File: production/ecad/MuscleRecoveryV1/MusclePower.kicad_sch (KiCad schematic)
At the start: 23 parts, among them IC1 LC709203FQH-01TWG, Q1 FDN340P, U1 AP1117-33, U2 MCP73831-2-OT

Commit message: rev1 first draft ready for review
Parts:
- removed R34, R35: 10K, symbol Device:R
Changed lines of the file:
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@@
   (junction (at 144.145 44.45) (diameter 0) (color 0 0 0 0)
   )
-  (junction (at 66.04 113.03) (diameter 0) (color 0 0 0 0)
-  )
   (junction (at 165.735 49.53) (diameter 0) (color 0 0 0 0)
   )
@@
   )
   (junction (at 95.25 51.7144) (diameter 0) (color 0 0 0 0)
-  )
-  (junction (at 69.85 115.57) (diameter 0) (color 0 0 0 0)
-  )
-  (junction (at 69.85 96.52) (diameter 0) (color 0 0 0 0)
   )
   (junction (at 50.8 54.0004) (diameter 0) (color 0 0 0 0)
@@
     (stroke (width 0) (type default))
   )
-  (wire (pts (xy 59.69 113.03) (xy 66.04 113.03))
+  (wire (pts (xy 59.69 113.03) (xy 71.12 113.03))
     (stroke (width 0) (type default))
   )
@@
     (stroke (width 0) (type default))
   )
-  (wire (pts (xy 66.04 113.03) (xy 71.12 113.03))
-    (stroke (width 0) (type default))
-  )
   (wire (pts (xy 36.83 114.3) (xy 36.83 116.84))
     (stroke (width 0) (type default))
@@
     (stroke (width 0) (type default))
   )
-  (wire (pts (xy 69.85 96.52) (xy 69.85 102.87))
-    (stroke (width 0) (type default))
-  )
   (wire (pts (xy 50.8 53.848) (xy 50.8 54.0004))
     (stroke (width 0) (type default))
@@
     (stroke (width 0) (type default))
   )
-  (wire (pts (xy 66.04 100.33) (xy 66.04 96.52))
-    (stroke (width 0) (type default))
-  )
   (wire (pts (xy 97.79 96.52) (xy 97.79 102.87))
     (stroke (width 0) (type default))
@@
     (stroke (width 0) (type default))
   )
-  (wire (pts (xy 66.04 107.95) (xy 66.04 113.03))
-    (stroke (width 0) (type default))
-  )
   (wire (pts (xy 27.94 65.6844) (xy 27.94 62.23))
     (stroke (width 0) (type default))
   )
-  (wire (pts (xy 69.85 115.57) (xy 71.12 115.57))
-    (stroke (width 0) (type default))
-  )
   (wire (pts (xy 71.12 120.65) (xy 67.31 120.65))
     (stroke (width 0) (type default))
@@
     (stroke (width 0) (type default))
   )
-  (wire (pts (xy 69.85 96.52) (xy 81.28 96.52))
-    (stroke (width 0) (type default))
-  )
-  (wire (pts (xy 66.04 96.52) (xy 69.85 96.52))
-    (stroke (width 0) (type default))
-  )
   (wire (pts (xy 46.99 116.84) (xy 46.99 121.92))
     (stroke (width 0) (type default))
@@
     (stroke (width 0) (type default))
   )
-  (wire (pts (xy 69.85 110.49) (xy 69.85 115.57))
-    (stroke (width 0) (type default))
-  )
   (wire (pts (xy 27.9908 48.26) (xy 43.18 48.26))
     (stroke (width 0) (type default))
@@
     (stroke (width 0) (type default))
   )
-  (wire (pts (xy 59.69 115.57) (xy 69.85 115.57))
+  (wire (pts (xy 59.69 115.57) (xy 71.12 115.57))
     (stroke (width 0) (type default))
   )
@@
         (path "/ec7ffed6-1d2d-48f7-b073-d0a7d4b8c858"
           (reference "#PWR04") (unit 1)
-        )
-      )
-    )
-  )
-  (symbol (lib_id "Device:R") (at 66.04 104.14 0) (unit 1)
-    (in_bom yes) (on_board yes) (dnp no)
-    (property "Reference" "R34" (at 62.23 102.87 0)
-      (effects (font (size 1.27 1.27)) (justify left))
-    )
-    (property "Value" "10K" (at 60.96 105.41 0)
-      (effects (font (size 1.27 1.27)) (justify left))
-    )
-    (property "Footprint" "" (at 64.262 104.14 90)
-      (effects (font (size 1.27 1.27)) hide)
-    )
-    (property "Datasheet" "~" (at 66.04 104.14 0)
-      (effects (font (size 1.27 1.27)) hide)
-    )
-    (pin "1")
-    (pin "2")
-    (instances
-      (project "MuscleRecoveryV1"
-        (path "/4e550305-79d2-4e4a-a502-817ebcc79f9a/648f095b-a230-48ff-8dbf-d0fbef398770"
-          (reference "R34") (unit 1)
         )
       )
@@
         )
       )
-    )
-  )
-  (symbol (lib_id "Device:R") (at 69.85 106.68 0) (unit 1)
-    (in_bom yes) (on_board yes) (dnp no)
-    (property "Reference" "R35" (at 71.12 105.41 0)
-      (effects (font (size 1.27 1.27)) (justify left))
-    )
-    (property "Value" "10K" (at 71.12 107.95 0)
-      (effects (font (size 1.27 1.27)) (justify left))
-    )
-    (property "Footprint" "" (at 68.072 106.68 90)
-      (effects (font (size 1.27 1.27)) hide)
-    )
-    (property "Datasheet" "~" (at 69.85 106.68 0)
-      (effects (font (size 1.27 1.27)) hide)
-    )
-    (pin "1")
-    (pin "2")
-    (instances
-      (project "MuscleRecoveryV1"
-        (path "/4e550305-79d2-4e4a-a502-817ebcc79f9a/648f095b-a230-48ff-8dbf-d0fbef398770"
-          (reference "R35") (unit 1)
-        )
-      )

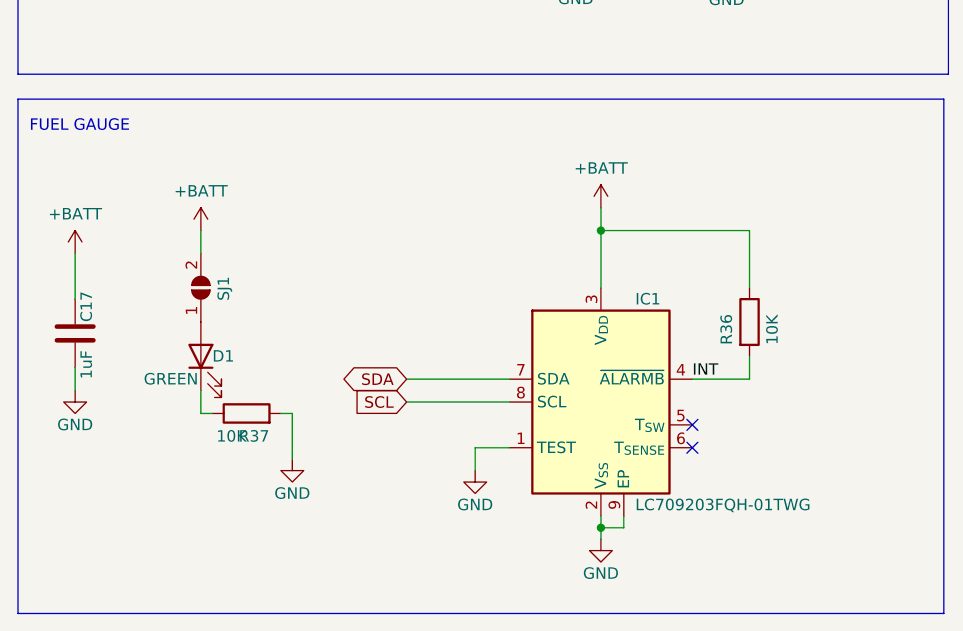
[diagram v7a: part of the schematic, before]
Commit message: updates from Sean's comments, some not all
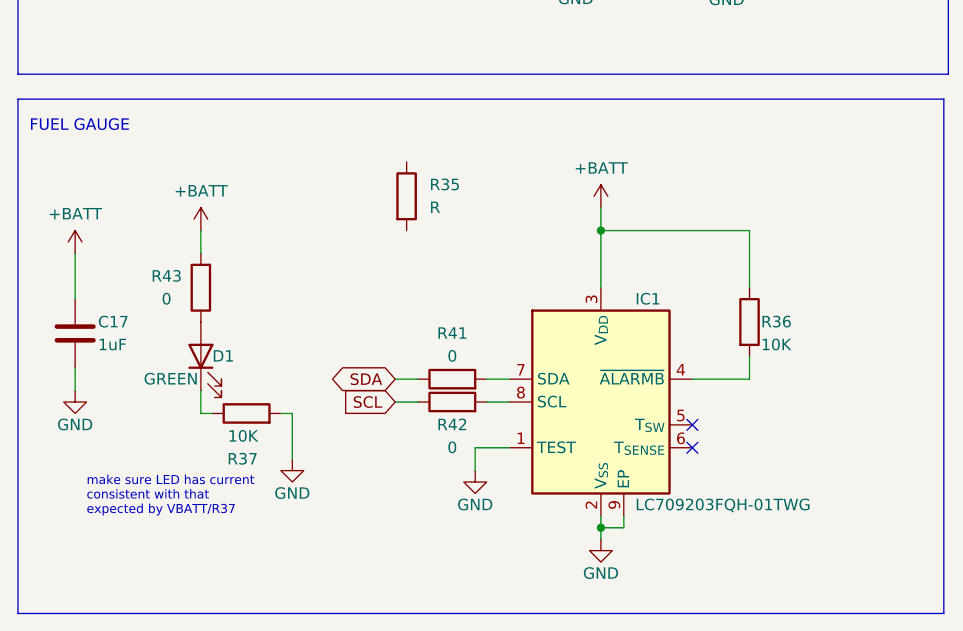
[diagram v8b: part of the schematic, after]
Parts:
- removed SJ1: SolderJumper_2_Open, symbol Jumper:SolderJumper_2_Open
- added R35: R, symbol Device:R
- added R41, R42, R43: 0, symbol Device:R
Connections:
- net +BATT: now also R43.2
- net SCL: now also R42.1; no longer IC1.8 (SCL)
- net SDA: now also R41.1; no longer IC1.7 (SDA)
- net at D1.2 (A): now also R43.1
- net INT: no longer names the net of IC1.4 (~{ALARMB}), R36.2
- new net: IC1.7 (SDA), R41.2
- new net: IC1.8 (SCL), R42.2
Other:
- note added: "make sure LED has current consistent with that expected by VBATT/R37"
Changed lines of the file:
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@@
-    (stroke (width 0) (type default))
-  )
-  (wire (pts (xy 59.69 113.03) (xy 71.12 113.03))
     (stroke (width 0) (type default))
   )
@@
     (stroke (width 0) (type default))
   )
+  (wire (pts (xy 68.58 113.03) (xy 71.12 113.03))
+    (stroke (width 0) (type default))
+  )
   (wire (pts (xy 95.25 60.96) (xy 95.25 66.04))
     (stroke (width 0) (type default))
@@
     (stroke (width 0) (type default))
   )
+  (wire (pts (xy 58.42 113.03) (xy 60.96 113.03))
+    (stroke (width 0) (type default))
+  )
   (wire (pts (xy 50.8 54.0004) (xy 69.342 54.0004))
     (stroke (width 0) (type default))
@@
     (stroke (width 0) (type default))
   )
+  (wire (pts (xy 68.58 115.57) (xy 71.12 115.57))
+    (stroke (width 0) (type default))
+  )
   (wire (pts (xy 27.94 65.6844) (xy 27.94 62.23))
     (stroke (width 0) (type default))
@@
     (stroke (width 0) (type default))
   )
+  (wire (pts (xy 58.42 115.57) (xy 60.96 115.57))
+    (stroke (width 0) (type default))
+  )
   (wire (pts (xy 46.99 116.84) (xy 46.99 121.92))
     (stroke (width 0) (type default))
@@
   )
   (wire (pts (xy 95.25 51.7144) (xy 95.25 55.88))
-    (stroke (width 0) (type default))
-  )
-  (wire (pts (xy 59.69 115.57) (xy 71.12 115.57))
     (stroke (width 0) (type default))
   )
@@
     (effects (font (size 1.27 1.27)) (justify left bottom))
   )
+  (text "make sure LED has current \nconsistent with that \nexpected by VBATT/R37"
+    (at 24.13 128.27 0)
+    (effects (font (size 1 1)) (justify left bottom))
+  )
   (text "Charging Circuitry\n" (at 126.365 20.701 0)
     (effects (font (size 1.27 1.27)) (justify left bottom))
   )
   (text "Power Selection Circuitry\n" (at 18.796 21.2344 0)
-    (effects (font (size 1.27 1.27)) (justify left bottom))
-  )
-  (label "INT" (at 91.44 113.03 0) (fields_autoplaced)
     (effects (font (size 1.27 1.27)) (justify left bottom))
   )
@@
     )
   )
-  (global_label "SDA" (shape bidirectional) (at 59.69 113.03 180) (fields_autoplaced)
+  (global_label "SDA" (shape bidirectional) (at 58.42 113.03 180) (fields_autoplaced)
     (effects (font (size 1.27 1.27)) (justify right))
-    (property "Intersheetrefs" "${INTERSHEET_REFS}" (at 52.0254 113.03 0)
+    (property "Intersheetrefs" "${INTERSHEET_REFS}" (at 50.7554 113.03 0)
       (effects (font (size 1.27 1.27)) (justify right) hide)
     )
@@
     )
   )
-  (global_label "SCL" (shape input) (at 59.69 115.57 180) (fields_autoplaced)
+  (global_label "SCL" (shape input) (at 58.42 115.57 180) (fields_autoplaced)
     (effects (font (size 1.27 1.27)) (justify right))
-    (property "Intersheetrefs" "${INTERSHEET_REFS}" (at 53.1972 115.57 0)
+    (property "Intersheetrefs" "${INTERSHEET_REFS}" (at 51.9272 115.57 0)
       (effects (font (size 1.27 1.27)) (justify right) hide)
     )
@@
     )
   )
+  (symbol (lib_id "Device:R") (at 64.77 113.03 90) (unit 1)
+    (in_bom yes) (on_board yes) (dnp no)
+    (property "Reference" "R41" (at 64.77 107.95 90)
+      (effects (font (size 1.27 1.27)))
+    )
+    (property "Value" "0" (at 64.77 110.49 90)
+      (effects (font (size 1.27 1.27)))
+    )
+    (property "Footprint" "" (at 64.77 114.808 90)
+      (effects (font (size 1.27 1.27)) hide)
+    )
+    (property "Datasheet" "~" (at 64.77 113.03 0)
+      (effects (font (size 1.27 1.27)) hide)
+    )
+    (pin "1")
+    (pin "2")
+    (instances
+      (project "MuscleRecoveryV1"
+        (path "/4e550305-79d2-4e4a-a502-817ebcc79f9a/648f095b-a230-48ff-8dbf-d0fbef398770"
+          (reference "R41") (unit 1)
+        )
+      )
+    )
+  )
   (symbol (lib_id "power:GND") (at 177.8 66.675 0) (unit 1)
     (in_bom yes) (on_board yes) (dnp no) (fields_autoplaced)
@@
         (path "/ec7ffed6-1d2d-48f7-b073-d0a7d4b8c858"
           (reference "#PWR026") (unit 1)
+        )
+      )
+    )
+  )
+  (symbol (lib_id "Device:R") (at 59.69 92.71 0) (unit 1)
+    (in_bom yes) (on_board yes) (dnp no) (fields_autoplaced)
+    (property "Reference" "R35" (at 62.23 91.44 0)
+      (effects (font (size 1.27 1.27)) (justify left))
+    )
+    (property "Value" "R" (at 62.23 93.98 0)
+      (effects (font (size 1.27 1.27)) (justify left))
+    )
+    (property "Footprint" "" (at 57.912 92.71 90)
+      (effects (font (size 1.27 1.27)) hide)
+    )
+    (property "Datasheet" "~" (at 59.69 92.71 0)
+      (effects (font (size 1.27 1.27)) hide)
+    )
+    (pin "1")
+    (pin "2")
+    (instances
+      (project "MuscleRecoveryV1"
+        (path "/4e550305-79d2-4e4a-a502-817ebcc79f9a/648f095b-a230-48ff-8dbf-d0fbef398770"
+          (reference "R35") (unit 1)
         )
       )
@@
   (symbol (lib_id "Device:R") (at 97.79 106.68 0) (unit 1)
     (in_bom yes) (on_board yes) (dnp no)
-    (property "Reference" "R36" (at 95.25 109.22 90)
-      (effects (font (size 1.27 1.27)) (justify left))
-    )
-    (property "Value" "10K" (at 100.33 109.22 90)
+    (property "Reference" "R36" (at 99.06 106.68 0)
+      (effects (font (size 1.27 1.27)) (justify left))
+    )
+    (property "Value" "10K" (at 99.06 109.22 0)
       (effects (font (size 1.27 1.27)) (justify left))
     )
@@
     )
   )
+  (symbol (lib_id "Device:R") (at 64.77 115.57 90) (unit 1)
+    (in_bom yes) (on_board yes) (dnp no)
+    (property "Reference" "R42" (at 64.77 118.11 90)
+      (effects (font (size 1.27 1.27)))
+    )
+    (property "Value" "0" (at 64.77 120.65 90)
+      (effects (font (size 1.27 1.27)))
+    )
+    (property "Footprint" "" (at 64.77 117.348 90)
+      (effects (font (size 1.27 1.27)) hide)
+    )
+    (property "Datasheet" "~" (at 64.77 115.57 0)
+      (effects (font (size 1.27 1.27)) hide)
+    )
+    (pin "1")
+    (pin "2")
+    (instances
+      (project "MuscleRecoveryV1"
+        (path "/4e550305-79d2-4e4a-a502-817ebcc79f9a/648f095b-a230-48ff-8dbf-d0fbef398770"
+          (reference "R42") (unit 1)
+        )
+      )
+    )
+  )
   (symbol (lib_id "power:+BATT") (at 50.8 37.0332 0) (unit 1)
     (in_bom yes) (on_board yes) (dnp no) (fields_autoplaced)
@@
     )
   )
+  (symbol (lib_id "Device:R") (at 36.83 102.87 180) (unit 1)
+    (in_bom yes) (on_board yes) (dnp no)
+    (property "Reference" "R43" (at 33.02 101.6 0)
+      (effects (font (size 1.27 1.27)))
+    )
+    (property "Value" "0" (at 33.02 104.14 0)
+      (effects (font (size 1.27 1.27)))
+    )
+    (property "Footprint" "" (at 38.608 102.87 90)
+      (effects (font (size 1.27 1.27)) hide)
+    )
+    (property "Datasheet" "~" (at 36.83 102.87 0)
+      (effects (font (size 1.27 1.27)) hide)
+    )
+    (pin "1")
+    (pin "2")
+    (instances
+      (project "MuscleRecoveryV1"
+        (path "/4e550305-79d2-4e4a-a502-817ebcc79f9a/648f095b-a230-48ff-8dbf-d0fbef398770"
+          (reference "R43") (unit 1)
+        )
+      )
+    )
+  )
   (symbol (lib_id "power:GND") (at 95.25 66.04 0) (unit 1)
     (in_bom yes) (on_board yes) (dnp no) (fields_autoplaced)
@@
   (symbol (lib_id "Device:C") (at 22.86 107.95 0) (unit 1)
     (in_bom yes) (on_board yes) (dnp no)
-    (property "Reference" "C17" (at 24.13 106.68 90)
-      (effects (font (size 1.27 1.27)) (justify left))
-    )
-    (property "Value" "1uF" (at 24.13 113.03 90)
+    (property "Reference" "C17" (at 25.4 106.68 0)
+      (effects (font (size 1.27 1.27)) (justify left))
+    )
+    (property "Value" "1uF" (at 25.4 109.22 0)
       (effects (font (size 1.27 1.27)) (justify left))
     )
@@
   (symbol (lib_id "Device:R") (at 41.91 116.84 90) (unit 1)
     (in_bom yes) (on_board yes) (dnp no)
-    (property "Reference" "R37" (at 44.45 119.38 90)
-      (effects (font (size 1.27 1.27)) (justify left))
-    )
-    (property "Value" "10K" (at 41.91 119.38 90)
+    (property "Reference" "R37" (at 43.18 121.92 90)
+      (effects (font (size 1.27 1.27)) (justify left))
+    )
+    (property "Value" "10K" (at 43.18 119.38 90)
       (effects (font (size 1.27 1.27)) (justify left))
     )
@@
         )
       )
-    )
-  )
-  (symbol (lib_id "Jumper:SolderJumper_2_Open") (at 36.83 102.87 90) (unit 1)
-    (in_bom yes) (on_board yes) (dnp no)
-    (property "Reference" "SJ1" (at 39.37 101.6 0)
-      (effects (font (size 1.27 1.27)) (justify right))
-    )
-    (property "Value" "SolderJumper_2_Open" (at 39.37 104.14 90)
-      (effects (font (size 1.27 1.27)) (justify right) hide)
-    )
-    (property "Footprint" "" (at 36.83 102.87 0)
-      (effects (font (size 1.27 1.27)) hide)
-    )
-    (property "Datasheet" "~" (at 36.83 102.87 0)
-      (effects (font (size 1.27 1.27)) hide)
-    )
-    (pin "1")
-    (pin "2")
-    (instances
-      (project "MuscleRecoveryV1"
-        (path "/4e550305-79d2-4e4a-a502-817ebcc79f9a/648f095b-a230-48ff-8dbf-d0fbef398770"
-          (reference "SJ1") (unit 1)
-        )
-      )
